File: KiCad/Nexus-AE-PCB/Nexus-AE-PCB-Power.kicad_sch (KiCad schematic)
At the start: 8 parts, among them J3 AE_BUS, Q1 AO3401

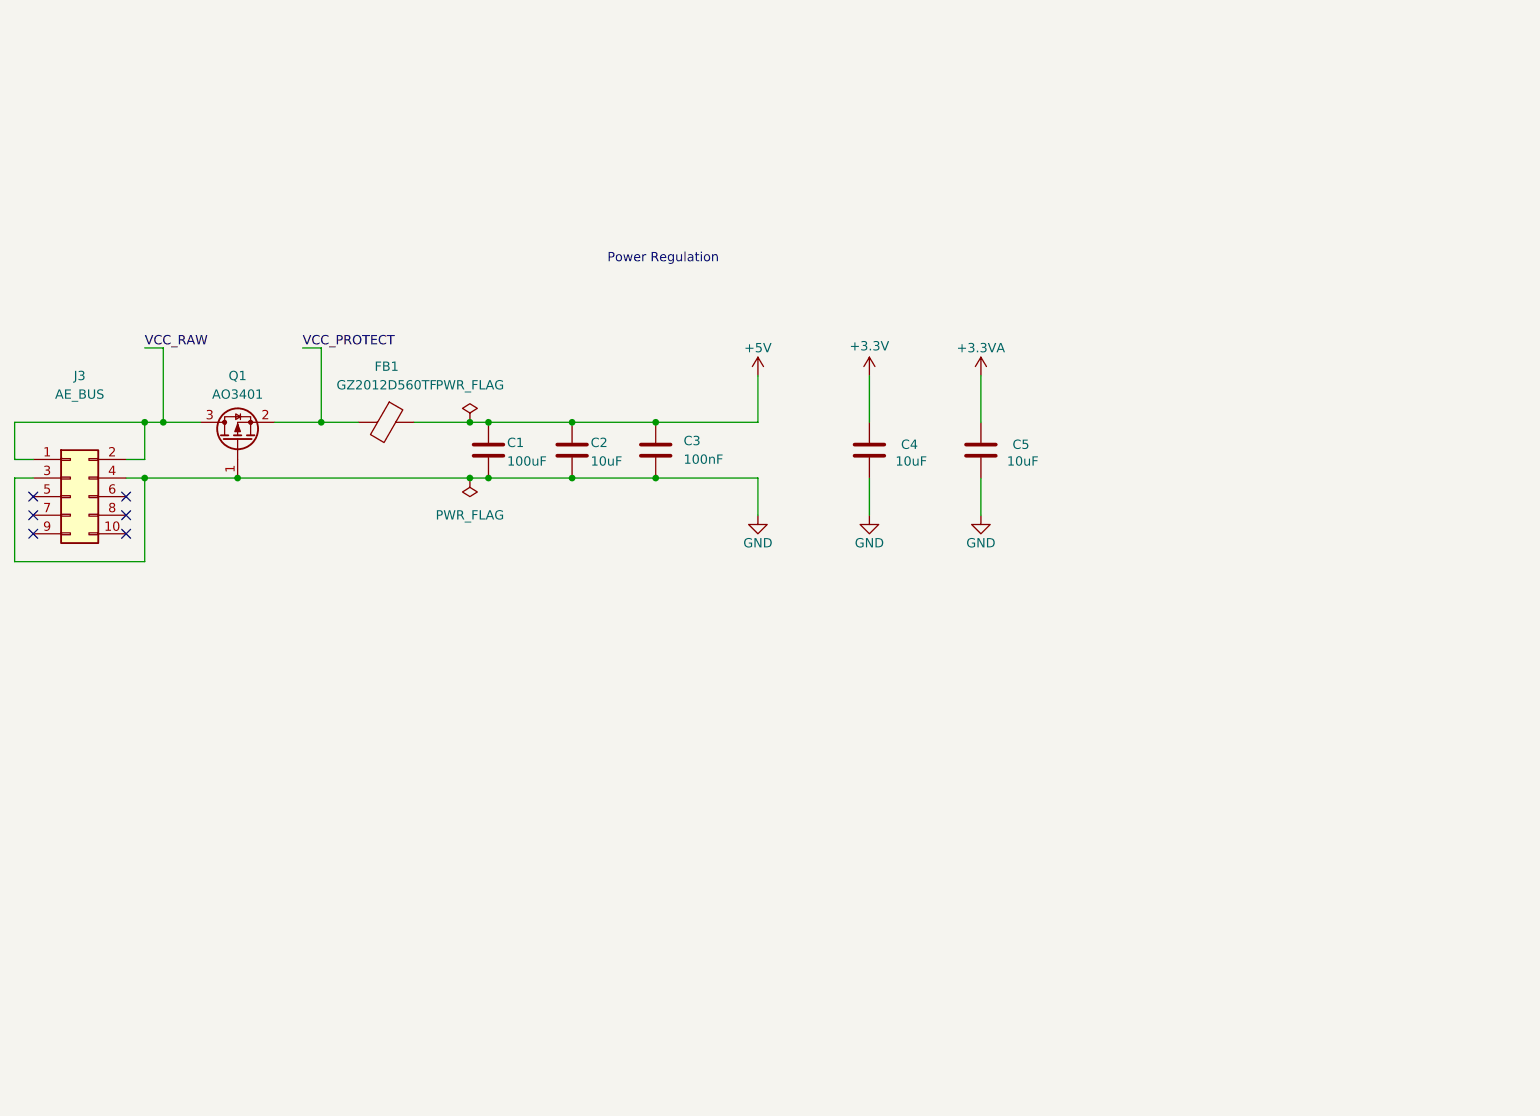
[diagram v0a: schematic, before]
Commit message: PCB and schmeatic are both approx 90% complete
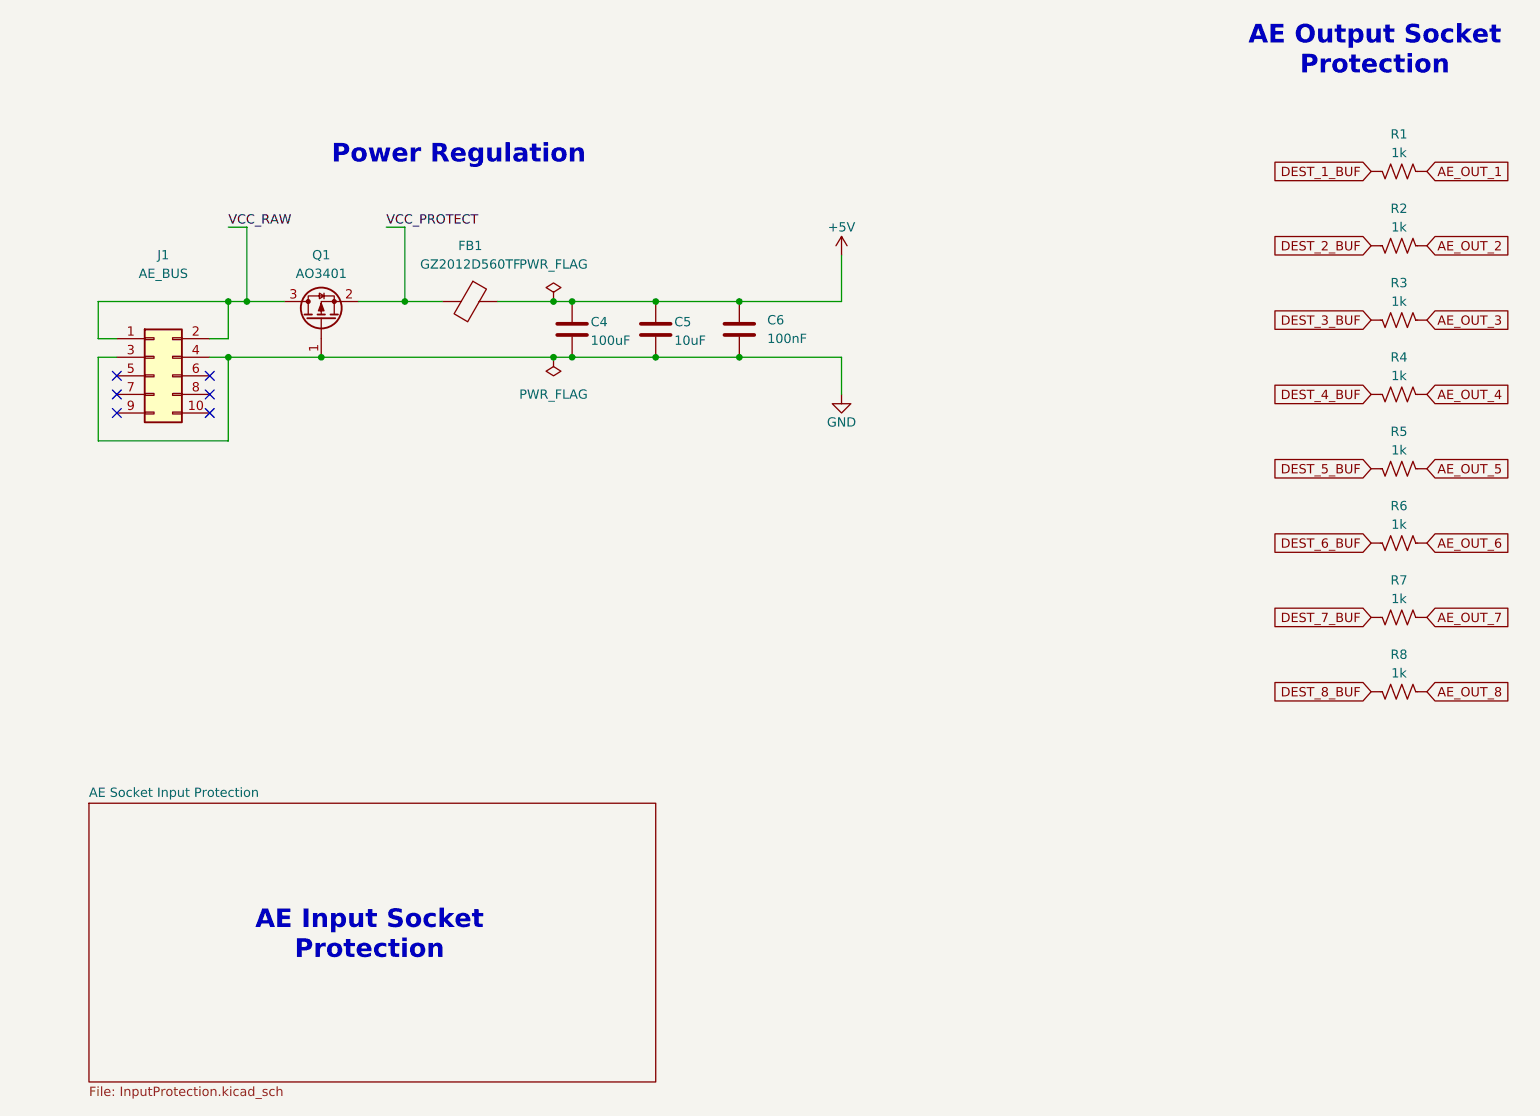
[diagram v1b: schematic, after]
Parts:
- removed C1: 100uF, Capacitor_SMD:C_0805_2012Metric, symbol Device:C
- removed C2: 10uF, Capacitor_SMD:C_0805_2012Metric, symbol Device:C
- removed C3: 100nF, Capacitor_SMD:C_0805_2012Metric, symbol Device:C
- removed J3: AE_BUS, Connector_PinHeader_2.54mm:PinHeader_2x05_P2.54mm_Vertical, symbol Connector_Generic:Conn_02x05_Odd_Even
- added C6: 100nF, Capacitor_SMD:C_0402_1005Metric, symbol Device:C
- added J1: AE_BUS, Connector_PinHeader_2.54mm:PinHeader_2x05_P2.54mm_Vertical, symbol Connector_Generic:Conn_02x05_Odd_Even
- added R1, R2, R3, R4, R5, R6, R7, R8: 1k, Resistor_SMD:R_0402_1005Metric, symbol Device:R_US
- C4: value 10uF -> 100uF; footprint Capacitor_SMD:C_0603_1608Metric -> Capacitor_SMD:C_0402_1005Metric
- C5: footprint Capacitor_SMD:C_0603_1608Metric -> Capacitor_SMD:C_0402_1005Metric
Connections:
- net +3.3V is gone; now on net GND: C4.2
- net +3.3VA is gone; now on net GND: C5.2
- net +5V: now also C4.1, C5.1, C6.1
- net GND: now also C6.2, J1.3 (Pin_3), J1.4 (Pin_4); no longer C4.1, C5.1
- net VCC_RAW: now also J1.1 (Pin_1), J1.2 (Pin_2)
- new net AE_OUT_1: R1.1
- new net AE_OUT_2: R2.1
- new net AE_OUT_3: R3.1
- new net AE_OUT_4: R4.1
- new net AE_OUT_5: R5.1
- new net AE_OUT_6: R6.1
- new net AE_OUT_7: R7.1
- new net AE_OUT_8: R8.1
- new net DEST_1_BUF: R1.2
- new net DEST_2_BUF: R2.2
- new net DEST_3_BUF: R3.2
- new net DEST_4_BUF: R4.2
- new net DEST_5_BUF: R5.2
- new net DEST_6_BUF: R6.2
- new net DEST_7_BUF: R7.2
- new net DEST_8_BUF: R8.2
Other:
- added sheet AE Socket Input Protection (InputProtection.kicad_sch)
- note added: "AE Input Socket Protection"
- note added: "AE Output Socket Protection"
